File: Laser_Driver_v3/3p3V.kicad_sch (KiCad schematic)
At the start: 16 parts, among them U5 MC7812CTG, U6 MC7805CTG, U7 LT3045EMSE 3.3V, U8 LP5907MFX-1.8

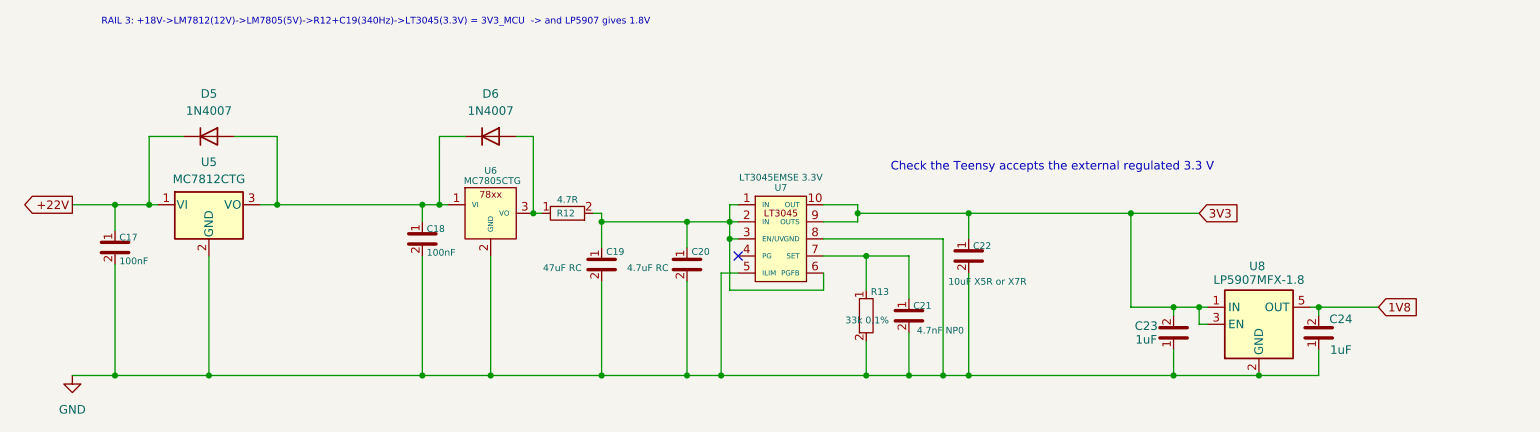
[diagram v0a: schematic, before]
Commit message: Updated the RF modulation implementation.
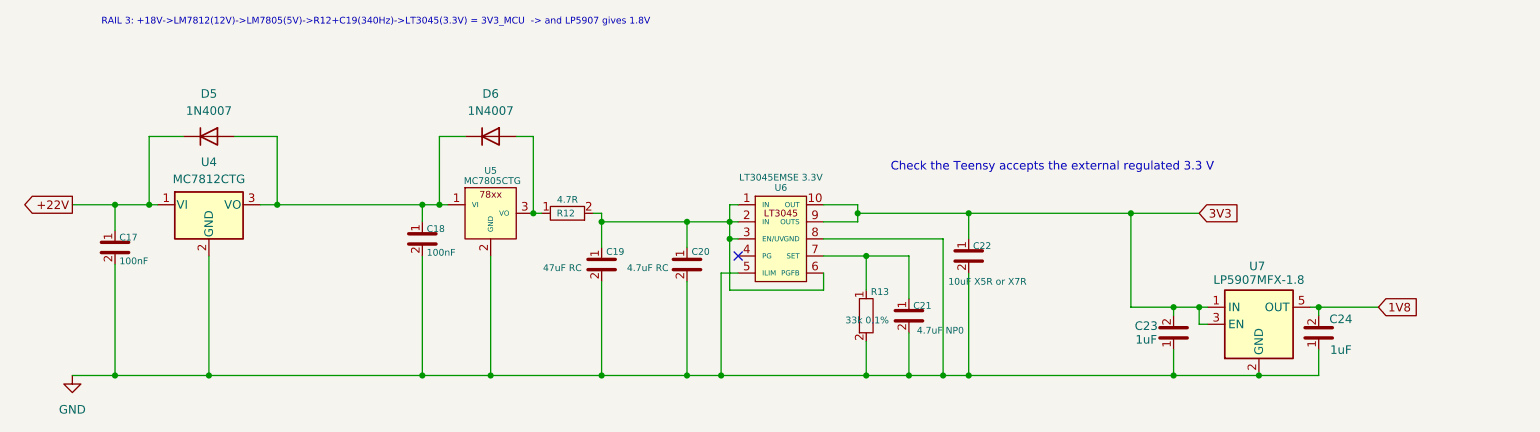
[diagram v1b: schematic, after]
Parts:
- C21: value 4.7nF NP0 -> 4.7uF NP0
- renumbered U5 to U4, U6 to U5, U7 to U6, U8 to U7
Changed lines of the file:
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@@
 		(in_pos_files yes)
 		(dnp no)
-		(property "Reference" "U8"
+		(property "Reference" "U7"
 			(at 230.886 65.024 0)
 			(show_name no)
@@
 			(project "laser_driver_v3"
 				(path "/b2c3d4e5-f6a7-8901-bcde-f12345678901/8f1d8420-6d65-4b14-9d89-baaedfa51091"
-					(reference "U8")
+					(reference "U7")
 					(unit 1)
 				)
@@
 		(in_pos_files yes)
 		(dnp no)
-		(property "Reference" "U6"
+		(property "Reference" "U5"
 			(at 116.84 50.8 0)
 			(show_name no)
@@
 			(project "laser_driver_v3"
 				(path "/b2c3d4e5-f6a7-8901-bcde-f12345678901/8f1d8420-6d65-4b14-9d89-baaedfa51091"
-					(reference "U6")
+					(reference "U5")
 					(unit 1)
 				)
@@
 			)
 		)
-		(property "Value" "4.7nF NP0"
+		(property "Value" "4.7uF NP0"
 			(at 183.75 74.582 0)
 			(show_name no)
@@
 		(in_pos_files yes)
 		(dnp no)
-		(property "Reference" "U7"
+		(property "Reference" "U6"
 			(at 160.02 53.34 0)
 			(show_name no)
@@
 			(project "laser_driver_v3"
 				(path "/b2c3d4e5-f6a7-8901-bcde-f12345678901/8f1d8420-6d65-4b14-9d89-baaedfa51091"
-					(reference "U7")
+					(reference "U6")
 					(unit 1)
 				)
@@
 		(dnp no)
 		(fields_autoplaced yes)
-		(property "Reference" "U5"
+		(property "Reference" "U4"
 			(at 74.93 49.53 0)
 			(show_name no)
@@
 			(project "laser_driver_v3"
 				(path "/b2c3d4e5-f6a7-8901-bcde-f12345678901/8f1d8420-6d65-4b14-9d89-baaedfa51091"
-					(reference "U5")
-					(unit 1)
-				)
+					(reference "U4")
+					(unit 1)
+				)

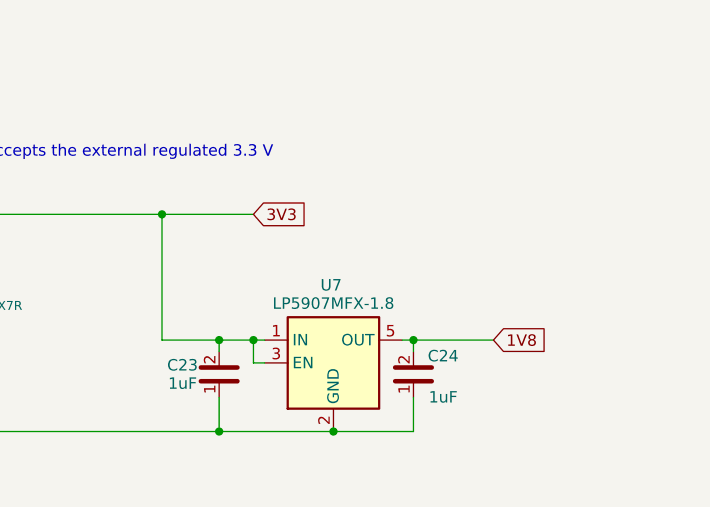
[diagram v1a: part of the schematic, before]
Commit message: Split into a power and signal board.
I think all footprints are now valid.  Need to figure out the power connections between boards, currently just screw terminals for wire.  I think a single multi-pin connector will work, but want to find something with premade off the shelf cables.
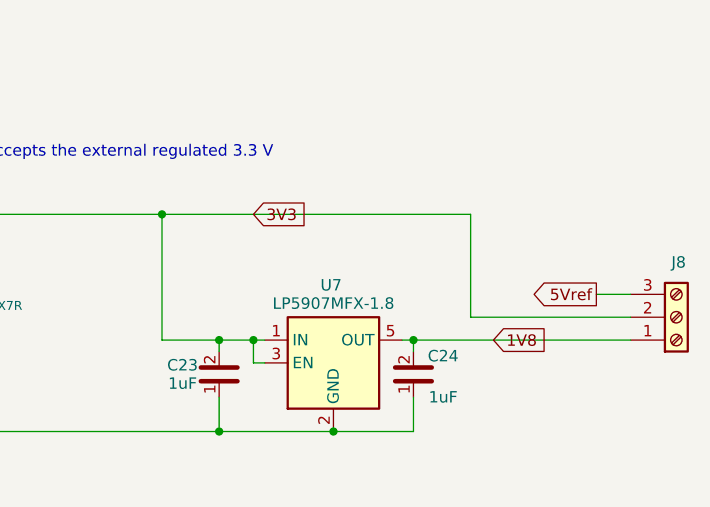
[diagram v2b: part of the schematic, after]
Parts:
- added J8: Screw_Terminal_01x03, Connector_Phoenix_MSTB:PhoenixContact_MSTBA_2,5_3-G-5,08_1x03_P5.08mm_Horizontal, symbol Connector:Screw_Terminal_01x03
- U6: footprint Package_SO:Analog_MSOP-12-16-1EP_3x4.039mm_P0.5mm_EP1.651x2.845mm_ThermalVias -> Package_SO:MSOP-12-1EP_3x4.039mm_P0.65mm_EP1.651x2.845mm_ThermalVias
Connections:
- net 1V8: now also J8.1 (Pin_1)
- net 3V3: now also J8.2 (Pin_2)
- new net 5Vref: J8.3 (Pin_3)
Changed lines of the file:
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@@
+	(wire
+		(pts
+			(xy 260.35 66.04) (xy 264.16 66.04)
+		)
+		(stroke
+			(width 0)
+			(type default)
+		)
+	)
 	(wire
 		(pts
@@
 	(wire
 		(pts
+			(xy 264.16 68.58) (xy 246.38 68.58)
+		)
+		(stroke
+			(width 0)
+			(type default)
+		)
+	)
+	(wire
+		(pts
 			(xy 82.55 55.88) (xy 85.09 55.88)
 		)
@@
 	(wire
 		(pts
-			(xy 240.03 71.12) (xy 248.92 71.12)
+			(xy 240.03 71.12) (xy 264.16 71.12)
 		)
 		(stroke
@@
 	(wire
 		(pts
+			(xy 246.38 68.58) (xy 246.38 57.15)
+		)
+		(stroke
+			(width 0)
+			(type default)
+		)
+	)
+	(wire
+		(pts
 			(xy 85.09 45.72) (xy 85.09 55.88)
 		)
@@
 	(wire
 		(pts
-			(xy 212.09 57.15) (xy 222.25 57.15)
+			(xy 212.09 57.15) (xy 246.38 57.15)
 		)
 		(stroke
@@
 		(property "Intersheetrefs" "${INTERSHEET_REFS}"
 			(at 46.5448 55.88 0)
+			(hide yes)
+			(show_name no)
+			(do_not_autoplace no)
+			(effects
+				(font
+					(size 1.27 1.27)
+				)
+				(justify right)
+			)
+		)
+	)
+	(global_label "5Vref"
+		(shape output)
+		(at 260.35 66.04 180)
+		(fields_autoplaced yes)
+		(effects
+			(font
+				(size 1.27 1.27)
+			)
+			(justify right)
+		)
+		(property "Intersheetrefs" "${INTERSHEET_REFS}"
+			(at 252.4662 66.04 0)
 			(hide yes)
 			(show_name no)
@@
 		)
 		(instances
-			(project "laser_driver_v3"
+			(project "laser_driver_v3_Power"
 				(path "/b2c3d4e5-f6a7-8901-bcde-f12345678901/8f1d8420-6d65-4b14-9d89-baaedfa51091"
 					(reference "C17")
@@
 		)
 		(instances
-			(project "laser_driver_v3"
+			(project "laser_driver_v3_Power"
 				(path "/b2c3d4e5-f6a7-8901-bcde-f12345678901/8f1d8420-6d65-4b14-9d89-baaedfa51091"
 					(reference "C20")
@@
 		)
 		(instances
-			(project "laser_driver_v3"
+			(project "laser_driver_v3_Power"
 				(path "/b2c3d4e5-f6a7-8901-bcde-f12345678901/8f1d8420-6d65-4b14-9d89-baaedfa51091"
 					(reference "C23")
@@
 		)
 		(instances
-			(project "laser_driver_v3"
+			(project "laser_driver_v3_Power"
 				(path "/b2c3d4e5-f6a7-8901-bcde-f12345678901/8f1d8420-6d65-4b14-9d89-baaedfa51091"
 					(reference "R13")
@@
 		)
 		(instances
-			(project "laser_driver_v3"
+			(project "laser_driver_v3_Power"
 				(path "/b2c3d4e5-f6a7-8901-bcde-f12345678901/8f1d8420-6d65-4b14-9d89-baaedfa51091"
 					(reference "D6")
@@
 		)
 		(instances
-			(project "laser_driver_v3"
+			(project "laser_driver_v3_Power"
 				(path "/b2c3d4e5-f6a7-8901-bcde-f12345678901/8f1d8420-6d65-4b14-9d89-baaedfa51091"
 					(reference "U7")
@@
 		)
 		(instances
-			(project "laser_driver_v3"
+			(project "laser_driver_v3_Power"
 				(path "/b2c3d4e5-f6a7-8901-bcde-f12345678901/8f1d8420-6d65-4b14-9d89-baaedfa51091"
 					(reference "D5")
@@
 		)
 		(instances
-			(project "laser_driver_v3"
+			(project "laser_driver_v3_Power"
 				(path "/b2c3d4e5-f6a7-8901-bcde-f12345678901/8f1d8420-6d65-4b14-9d89-baaedfa51091"
 					(reference "U5")
@@
 		)
 		(instances
-			(project "laser_driver_v3"
+			(project "laser_driver_v3_Power"
 				(path "/b2c3d4e5-f6a7-8901-bcde-f12345678901/8f1d8420-6d65-4b14-9d89-baaedfa51091"
 					(reference "C22")
@@
 		)
 		(instances
-			(project "laser_driver_v3"
+			(project "laser_driver_v3_Power"
 				(path "/b2c3d4e5-f6a7-8901-bcde-f12345678901/8f1d8420-6d65-4b14-9d89-baaedfa51091"
 					(reference "C18")
@@
 		)
 		(instances
-			(project "laser_driver_v3"
+			(project "laser_driver_v3_Power"
 				(path "/b2c3d4e5-f6a7-8901-bcde-f12345678901/8f1d8420-6d65-4b14-9d89-baaedfa51091"
 					(reference "R12")
+					(unit 1)
+				)
+			)
+		)
+	)
+	(symbol
+		(lib_id "Connector:Screw_Terminal_01x03")
+		(at 269.24 68.58 0)
+		(mirror x)
+		(unit 1)
+		(body_style 1)
+		(exclude_from_sim no)
+		(in_bom yes)
+		(on_board yes)
+		(in_pos_files yes)
+		(dnp no)
+		(property "Reference" "J8"
+			(at 269.494 62.484 0)
+			(show_name no)
+			(do_not_autoplace no)
+			(effects
+				(font
+					(size 1.27 1.27)
+				)
+			)
+		)
+		(property "Value" "Screw_Terminal_01x03"
+			(at 269.24 62.23 0)
+			(hide yes)
+			(show_name no)
+			(do_not_autoplace no)
+			(effects
+				(font
+					(size 1.27 1.27)
+				)
+			)
+		)
+		(property "Footprint" "Connector_Phoenix_MSTB:PhoenixContact_MSTBA_2,5_3-G-5,08_1x03_P5.08mm_Horizontal"
+			(at 269.24 68.58 0)
+			(hide yes)
+			(show_name no)
+			(do_not_autoplace no)
+			(effects
+				(font
+					(size 1.27 1.27)
+				)
+			)
+		)
+		(property "Datasheet" ""
+			(at 269.24 68.58 0)
+			(hide yes)
+			(show_name no)
+			(do_not_autoplace no)
+			(effects
+				(font
+					(size 1.27 1.27)
+				)
+			)
+		)
+		(property "Description" "Generic screw terminal, single row, 01x03, script generated (kicad-library-utils/schlib/autogen/connector/)"
+			(at 269.24 68.58 0)
+			(hide yes)
+			(show_name no)
+			(do_not_autoplace no)
+			(effects
+				(font
+					(size 1.27 1.27)
+				)
+			)
+		)
+		(pin "1"
+		)
+		(pin "2"
+		)
+		(pin "3"
+		)
+		(instances
+			(project "laser_driver_v3_Power"
+				(path "/b2c3d4e5-f6a7-8901-bcde-f12345678901/8f1d8420-6d65-4b14-9d89-baaedfa51091"
+					(reference "J8")
 					(unit 1)
 				)
@@
 		)
 		(instances
-			(project "laser_driver_v3"
+			(project "laser_driver_v3_Power"
 				(path "/b2c3d4e5-f6a7-8901-bcde-f12345678901/8f1d8420-6d65-4b14-9d89-baaedfa51091"
 					(reference "C21")
@@
 		)
 		(instances
-			(project "laser_driver_v3"
+			(project "laser_driver_v3_Power"
 				(path "/b2c3d4e5-f6a7-8901-bcde-f12345678901/8f1d8420-6d65-4b14-9d89-baaedfa51091"
 					(reference "C19")
@@
 			)
 		)
-		(property "Footprint" "Package_SO:Analog_MSOP-12-16-1EP_3x4.039mm_P0.5mm_EP1.651x2.845mm_ThermalVias"
+		(property "Footprint" "Package_SO:MSOP-12-1EP_3x4.039mm_P0.65mm_EP1.651x2.845mm_ThermalVias"
 			(at 80.02 37.69 0)
 			(hide yes)
@@
 		)
 		(instances
-			(project "laser_driver_v3"
+			(project "laser_driver_v3_Power"
 				(path "/b2c3d4e5-f6a7-8901-bcde-f12345678901/8f1d8420-6d65-4b14-9d89-baaedfa51091"
 					(reference "U6")
@@
 		)
 		(instances
-			(project "laser_driver_v3"
+			(project "laser_driver_v3_Power"
 				(path "/b2c3d4e5-f6a7-8901-bcde-f12345678901/8f1d8420-6d65-4b14-9d89-baaedfa51091"
 					(reference "U4")
@@
 		)
 		(instances
-			(project "laser_driver_v3"
+			(project "laser_driver_v3_Power"
 				(path "/b2c3d4e5-f6a7-8901-bcde-f12345678901/8f1d8420-6d65-4b14-9d89-baaedfa51091"
 					(reference "#PWR09")
@@
 		)
 		(instances
-			(project "laser_driver_v3"
+			(project "laser_driver_v3_Power"
 				(path "/b2c3d4e5-f6a7-8901-bcde-f12345678901/8f1d8420-6d65-4b14-9d89-baaedfa51091"
 					(reference "C24")

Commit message: First power pcb layout without traces.
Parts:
- removed J8: Screw_Terminal_01x03, Connector_Phoenix_MSTB:PhoenixContact_MSTBA_2,5_3-G-5,08_1x03_P5.08mm_Horizontal, symbol Connector:Screw_Terminal_01x03
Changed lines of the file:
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@@
+	)
+	(junction
+		(at 60.96 55.88)
+		(diameter 0)
+		(color 0 0 0 0)
+	)
+	(junction
+		(at 218.44 81.28)
+		(diameter 0)
+		(color 0 0 0 0)
+	)
+	(junction
+		(at 133.35 81.28)
+		(diameter 0)
+		(color 0 0 0 0)
+	)
+	(junction
+		(at 66.04 55.88)
+		(diameter 0)
+		(color 0 0 0 0)
+	)
+	(junction
+		(at 218.44 71.12)
+		(diameter 0)
+		(color 0 0 0 0)
+	)
+	(junction
+		(at 222.25 71.12)
+		(diameter 0)
+		(color 0 0 0 0)
 	)
 	(junction
@@
 	)
 	(junction
-		(at 60.96 55.88)
-		(diameter 0)
-		(color 0 0 0 0)
-	)
-	(junction
-		(at 218.44 81.28)
+		(at 152.4 60.96)
+		(diameter 0)
+		(color 0 0 0 0)
+	)
+	(junction
+		(at 123.19 57.15)
 		(diameter 0)
 		(color 0 0 0 0)
@@
 	(junction
 		(at 212.09 57.15)
-		(diameter 0)
-		(color 0 0 0 0)
-	)
-	(junction
-		(at 133.35 81.28)
-		(diameter 0)
-		(color 0 0 0 0)
-	)
-	(junction
-		(at 66.04 55.88)
-		(diameter 0)
-		(color 0 0 0 0)
-	)
-	(junction
-		(at 218.44 71.12)
-		(diameter 0)
-		(color 0 0 0 0)
-	)
-	(junction
-		(at 222.25 71.12)
-		(diameter 0)
-		(color 0 0 0 0)
-	)
-	(junction
-		(at 152.4 60.96)
-		(diameter 0)
-		(color 0 0 0 0)
-	)
-	(junction
-		(at 123.19 57.15)
 		(diameter 0)
 		(color 0 0 0 0)
@@
 	(wire
 		(pts
-			(xy 260.35 66.04) (xy 264.16 66.04)
-		)
-		(stroke
-			(width 0)
-			(type default)
-		)
-	)
-	(wire
-		(pts
 			(xy 133.35 67.31) (xy 133.35 81.28)
 		)
@@
 	(wire
 		(pts
-			(xy 264.16 68.58) (xy 246.38 68.58)
-		)
-		(stroke
-			(width 0)
-			(type default)
-		)
-	)
-	(wire
-		(pts
 			(xy 82.55 55.88) (xy 85.09 55.88)
 		)
@@
 	(wire
 		(pts
-			(xy 240.03 71.12) (xy 264.16 71.12)
+			(xy 212.09 57.15) (xy 222.25 57.15)
 		)
 		(stroke
@@
 	(wire
 		(pts
-			(xy 246.38 68.58) (xy 246.38 57.15)
-		)
-		(stroke
-			(width 0)
-			(type default)
-		)
-	)
-	(wire
-		(pts
 			(xy 85.09 45.72) (xy 85.09 55.88)
 		)
@@
 	(wire
 		(pts
-			(xy 212.09 57.15) (xy 246.38 57.15)
-		)
-		(stroke
-			(width 0)
-			(type default)
-		)
-	)
-	(wire
-		(pts
 			(xy 240.03 77.47) (xy 240.03 81.28)
 		)
@@
 		(pts
 			(xy 60.96 55.88) (xy 66.04 55.88)
+		)
+		(stroke
+			(width 0)
+			(type default)
+		)
+	)
+	(wire
+		(pts
+			(xy 240.03 71.12) (xy 248.92 71.12)
 		)
 		(stroke
@@
 		(property "Intersheetrefs" "${INTERSHEET_REFS}"
 			(at 46.5448 55.88 0)
-			(hide yes)
-			(show_name no)
-			(do_not_autoplace no)
-			(effects
-				(font
-					(size 1.27 1.27)
-				)
-				(justify right)
-			)
-		)
-	)
-	(global_label "5Vref"
-		(shape output)
-		(at 260.35 66.04 180)
-		(fields_autoplaced yes)
-		(effects
-			(font
-				(size 1.27 1.27)
-			)
-			(justify right)
-		)
-		(property "Intersheetrefs" "${INTERSHEET_REFS}"
-			(at 252.4662 66.04 0)
 			(hide yes)
 			(show_name no)
@@
 					(unit 1)
 				)
-			)
-		)
-	)
-	(symbol
-		(lib_id "Connector:Screw_Terminal_01x03")
-		(at 269.24 68.58 0)
-		(mirror x)
-		(unit 1)
-		(body_style 1)
-		(exclude_from_sim no)
-		(in_bom yes)
-		(on_board yes)
-		(in_pos_files yes)
-		(dnp no)
-		(property "Reference" "J8"
-			(at 269.494 62.484 0)
-			(show_name no)
-			(do_not_autoplace no)
-			(effects
-				(font
-					(size 1.27 1.27)
-				)
-			)
-		)
-		(property "Value" "Screw_Terminal_01x03"
-			(at 269.24 62.23 0)
-			(hide yes)
-			(show_name no)
-			(do_not_autoplace no)
-			(effects
-				(font
-					(size 1.27 1.27)
-				)
-			)
-		)
-		(property "Footprint" "Connector_Phoenix_MSTB:PhoenixContact_MSTBA_2,5_3-G-5,08_1x03_P5.08mm_Horizontal"
-			(at 269.24 68.58 0)
-			(hide yes)
-			(show_name no)
-			(do_not_autoplace no)
-			(effects
-				(font
-					(size 1.27 1.27)
-				)
-			)
-		)
-		(property "Datasheet" ""
-			(at 269.24 68.58 0)
-			(hide yes)
-			(show_name no)
-			(do_not_autoplace no)
-			(effects
-				(font
-					(size 1.27 1.27)
-				)
-			)
-		)
-		(property "Description" "Generic screw terminal, single row, 01x03, script generated (kicad-library-utils/schlib/autogen/connector/)"
-			(at 269.24 68.58 0)
-			(hide yes)
-			(show_name no)
-			(do_not_autoplace no)
-			(effects
-				(font
-					(size 1.27 1.27)
-				)
-			)
-		)
-		(pin "1"
-		)
-		(pin "2"
-		)
-		(pin "3"
-		)
-		(instances
-			(project "laser_driver_v3_Power"
-				(path "/b2c3d4e5-f6a7-8901-bcde-f12345678901/8f1d8420-6d65-4b14-9d89-baaedfa51091"
-					(reference "J8")
-					(unit 1)
-				)

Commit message: Started working on routing.
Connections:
- net GND: now also U6.13 (GND)
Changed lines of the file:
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@@
 		(pin "9"
+		)
+		(pin "13"
 		)
 		(instances

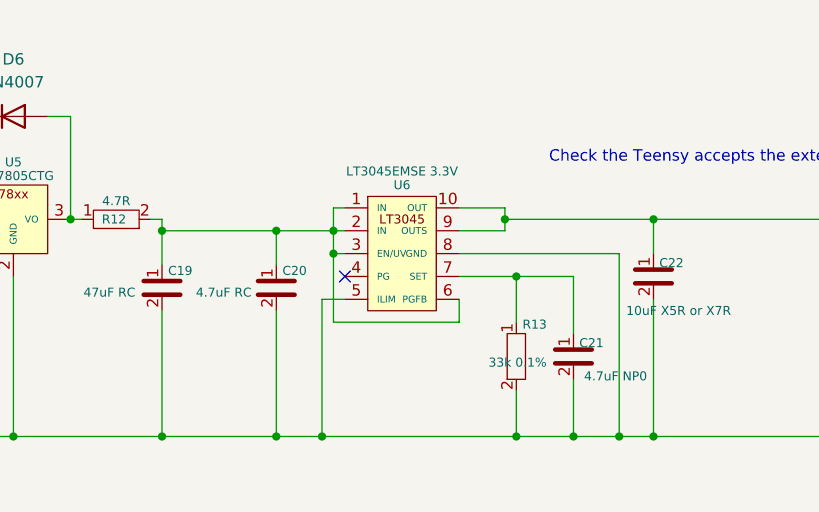
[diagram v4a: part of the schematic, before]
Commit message: Updated LT3045 footprints started Cu pours
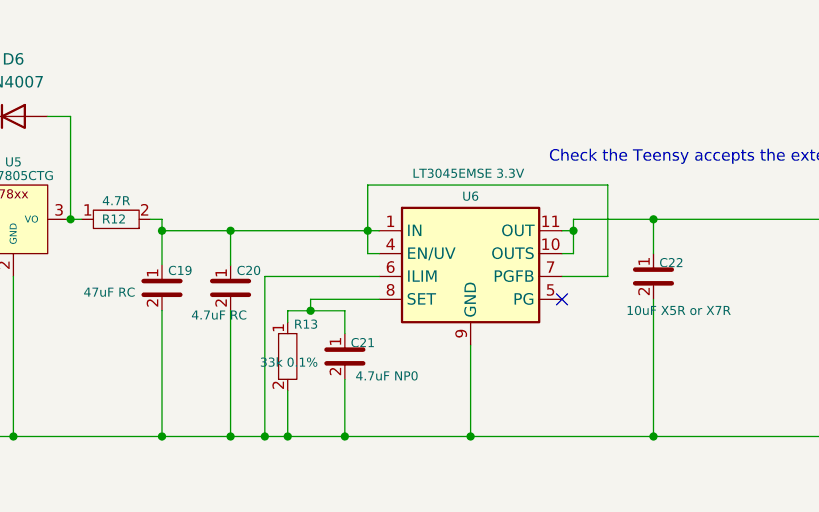
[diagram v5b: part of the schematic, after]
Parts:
- U6: footprint Package_SO:MSOP-12-1EP_3x4.039mm_P0.65mm_EP1.651x2.845mm_ThermalVias -> Package_SO:MSOP-12-1EP_3x4.039mm_P0.65mm_EP1.651x2.845mm; symbol Regulator_Linear:LT3042 -> Regulator_Linear:LT3045xMSE
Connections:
- net 3V3: now also U6.11 (OUT), U6.12 (OUT); no longer U6.9 (OUTS)
- net GND: now also U6.6 (ILIM), U6.9 (GND); no longer U6.5 (ILIM), U6.8 (GND)
- net at C19.1, C20.1, R12.2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: now also U6.4 (EN/UV), U6.7 (PGFB); no longer U6.6 (PGFB)
- net at C21.1, R13.1: now also U6.8 (SET); no longer U6.7 (SET)
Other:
- moved on the sheet: C20, C21, R13

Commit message: updated to newer/available parts
Routing needs to be completely redone.
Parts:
- C21: value 4.7uF NP0 -> 4.7uF X7R
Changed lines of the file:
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@@
 			)
 		)
-		(property "Value" "4.7uF NP0"
+		(property "Value" "4.7uF X7R"
 			(at 158.35 74.582 0)
 			(show_name no)
